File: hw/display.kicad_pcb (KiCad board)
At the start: 2 copper layers, 115.4 x 69.3 mm, 64 parts, among them J1 AMPSEAL_14_POS_776261-1_V, J2 ARM_JTAG_SWD_HEADER_10_PINSMD, J3 HEADER_USART_2_SMD, J4 HEADER_MOLEX_52207-0433, J5 HEADER_MOLEX_54104-4031, U1 MCP2551_SOIC8, U2 ALLIANCE_AS4C4M16SA_TSOP_II, U3 WINDBOND_W25Q32FV_SOIC8_W, U4 LPC1785FBD208_551QFP50, U5 MOSFET-N_2N7002W, U6 MOSFET-N_2N7002W, X1 XTAL_7A-20.000MAAJ-T, X2 XTAL_ABS25-32.768KHZ-T, X3 BUZZER_PKM13EPYH4002-B0

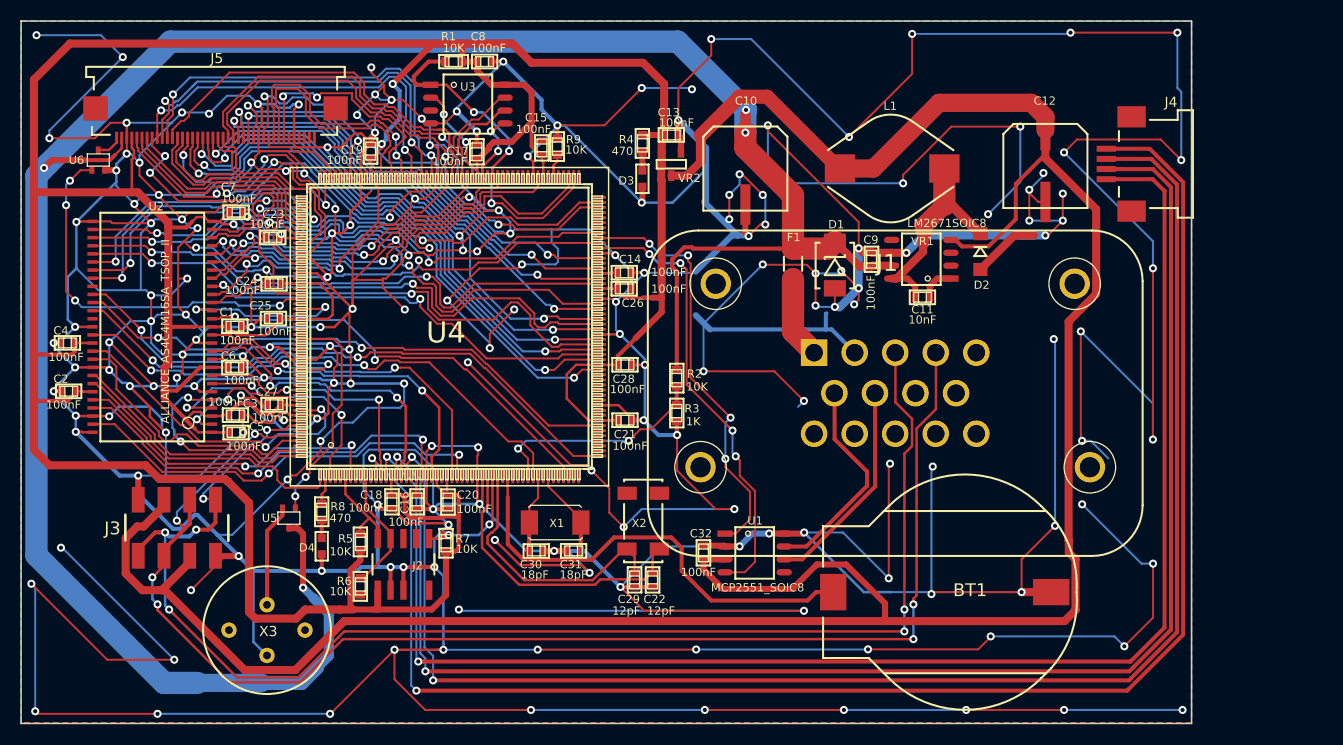
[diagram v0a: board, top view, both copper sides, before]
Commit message: PCB was too big for itead, reduced size and ordered one
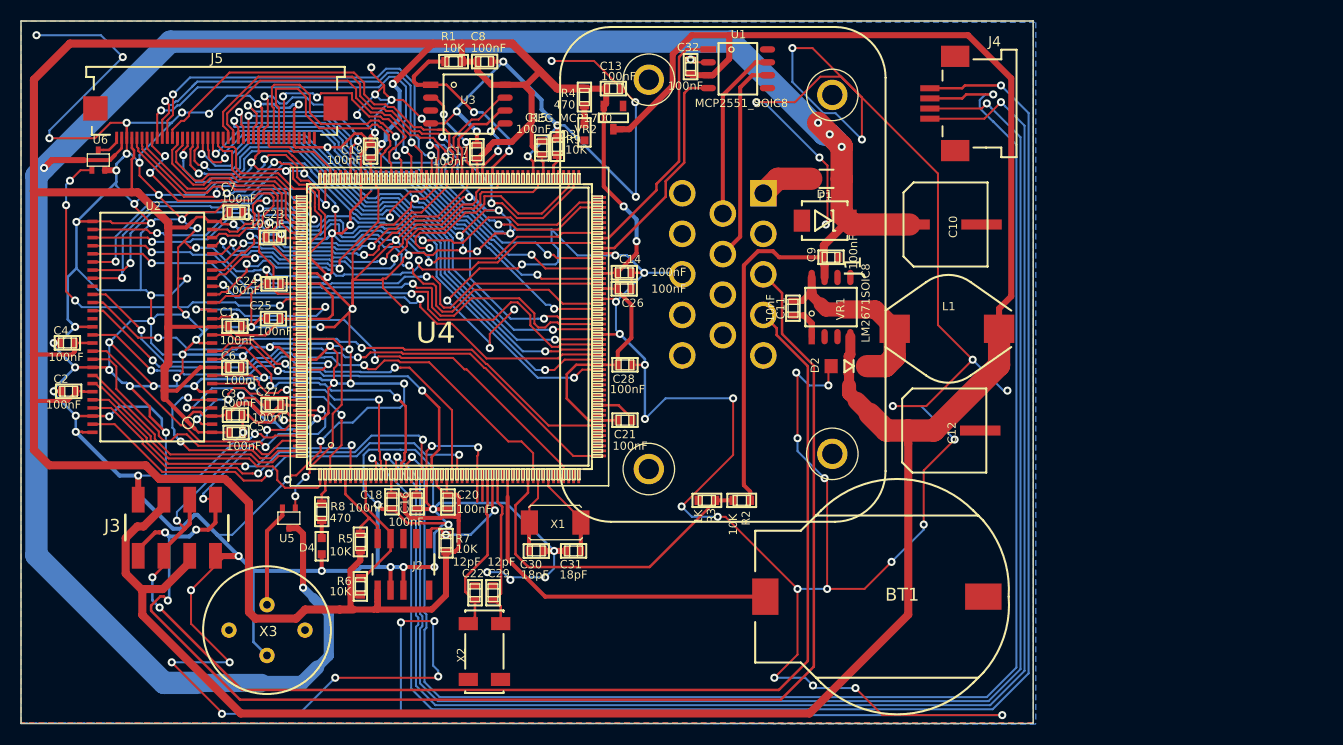
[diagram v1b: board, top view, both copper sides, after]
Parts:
- C10, C12: footprint usevolt:usevolt-CAP_EEE-FK1H470P -> usevolt:CAP_EEE-FK1H470P
- D1: footprint usevolt:usevolt-DO-214AA -> usevolt:DO-214AA
- D2: footprint usevolt:usevolt-DO219AB -> usevolt:DO219AB
- F1: footprint usevolt:usevolt-FUSE_MC36211 -> usevolt:FUSE_MC36211
- J3: footprint usevolt:usevolt-HEADER_4_2_SMD -> usevolt:HEADER_4_2_SMD
- L1: footprint usevolt:usevolt-INDUCTOR_BOURNS_10X13X5MM -> usevolt:INDUCTOR_BOURNS_10X13X5MM
- U1, VR1: footprint usevolt:usevolt-SOIC8 -> usevolt:SOIC8
- U2: footprint usevolt:usevolt-TSOP_II_54_PIN -> usevolt:TSOP_II_54_PIN
- U3: footprint usevolt:usevolt-SOIC8_W -> usevolt:SOIC8_W
- U4: footprint usevolt:usevolt-QFP208 -> usevolt:QFP208
- U5, U6: footprint usevolt:usevolt-SOT323 -> usevolt:SOT323
- VR2: footprint usevolt:usevolt-SOT-23_3-PIN -> usevolt:SOT-23_3-PIN
- X1: footprint usevolt:usevolt-XTAL_7A-20.000MAJ -> usevolt:XTAL_7A-20.000MAJ
- X2: footprint usevolt:usevolt-XTAL_32.768KHZ-T -> usevolt:XTAL_32.768KHZ-T
- moved C32 48.0 mm to (148.6, 60.4)
- moved U1 47.8 mm to (153.2, 60.6)
- moved C12 27.9 mm to (173.6, 96.3), turned to 270 degrees
- moved J1 20.6 mm to (151.8, 80.9), turned to 270 degrees
- moved C10 20.5 mm to (173.7, 75.9), turned to 270 degrees
- moved X2 20.3 mm to (128.2, 118.1), turned to 270 degrees
- moved J4 18.4 mm to (176.5, 64.0)
- moved C22 17.6 mm to (127.3, 112.3), turned to 270 degrees
- moved D2 17.2 mm to (164.2, 89.9), turned to 0 degrees
- moved L1 16.7 mm to (173.9, 86.2), turned to 0 degrees
- moved C29 14.0 mm to (129.1, 112.3), turned to 270 degrees
- moved R2 13.7 mm to (153.6, 103.2), turned to 0 degrees
- moved C11 12.8 mm to (158.7, 84.2), turned to 90 degrees
- moved VR1 10.1 mm to (162.4, 84.1), turned to 90 degrees
- moved R3 9.11 mm to (150.2, 103.2), turned to 0 degrees
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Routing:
- net GND: track 1826.5 -> 1303.4 mm, vias 194 -> 148
- net +5V: track 257.6 -> 230.1 mm
- net /lpc1785_sheet/CAN_RXD: track 44.6 -> 22.3 mm, vias 4 -> 0
- net VDD: track 225.3 -> 243.5 mm, vias 4 -> 5
- net /lpc1785_sheet/CAN_TXD: track 41.6 -> 24.9 mm, vias 4 -> 0
- net +3V3: track 419.3 -> 406.3 mm, vias 4 -> 6
- net /lpc1785_sheet/RTC_X1: track 28.8 -> 16.4 mm
- net /lpc1785_sheet/RTC_X2: track 26.3 -> 15.5 mm
- net /lpc1785_sheet/VDD_SENSE: track 22.3 -> 33.0 mm, vias 2 -> 0
- net /lpc1785_sheet/RTC_BAT: track 44.6 -> 35.2 mm
- net /lpc1785_sheet/TXD: track 139.8 -> 146.5 mm, vias 7 -> 5
- net /lpc1785_sheet/LCD_X_L: track 147.7 -> 152.8 mm
- net /lpc1785_sheet/RXD: track 138.6 -> 134.4 mm, vias 6 -> 4
- net /CANH: track 21.1 -> 17.4 mm
- net /pwr_supply_sheet/VIN: track 8.14 -> 5.32 mm
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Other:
- board size 115.4 x 69.3 mm -> 99.8 x 69.3 mm

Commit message: Changed LCD interface from RGB888 to RGB565
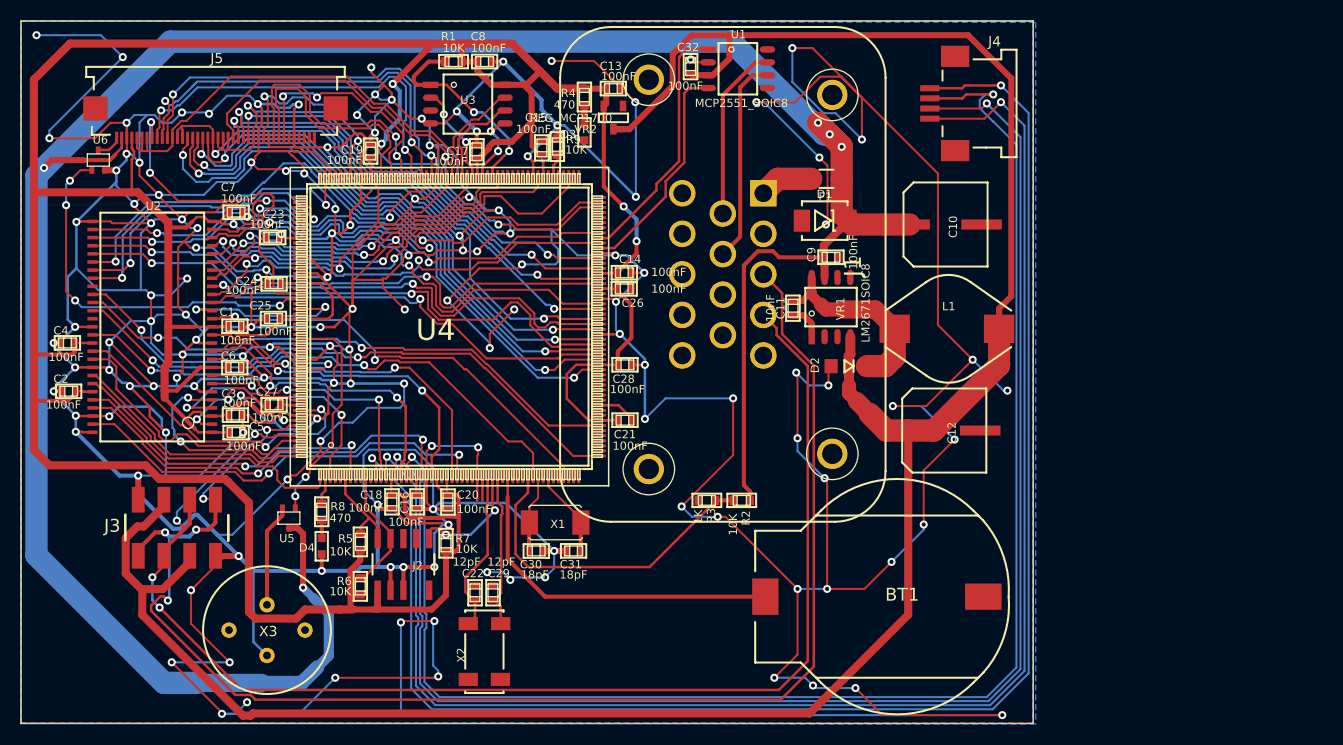
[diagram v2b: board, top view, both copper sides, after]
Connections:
- net /VD10 renamed /G0
- net /VD11 renamed /G1
- net /VD12 renamed /G2
- net /VD13 renamed /G3
- net /VD14 renamed /G4
- net /VD19 renamed /B0
- net /VD20 renamed /B1
- net /VD21 renamed /B2
- net /VD22 renamed /B3
- net /VD3 renamed /R0
- net /VD4 renamed /R1
- net /VD5 renamed /R2
- net /VD6 renamed /R3
- J5 pad 12: /VD7 -> /R4
- J5 pad 13: /VD8 -> /G5
- J5 pad 14: /VD9 -> /G5
- J5 pad 20: /VD15 -> /G5
- J5 pad 21: /VD16 -> /B4
- J5 pad 22: /VD17 -> /B4
- J5 pad 23: /VD18 -> /B4
- J5 pad 28: /VD23 -> /B4
- J5 pad 5: /VD0 -> /R4
- J5 pad 6: /VD1 -> /R4
- J5 pad 7: /VD2 -> /R4
- U4 pad 106: /VD18 -> (no net)
- U4 pad 132: /VD7 -> /R4
- U4 pad 158: /VD17 -> (no net)
- U4 pad 160: /VD16 -> (no net)
- U4 pad 162: /VD9 -> (no net)
- U4 pad 164: /VD8 -> (no net)
- U4 pad 166: /VD1 -> (no net)
- U4 pad 168: /VD0 -> (no net)
- U4 pad 170: /VD2 -> (no net)
- U4 pad 80: /VD15 -> /G5
- U4 pad 92: /VD23 -> /B4
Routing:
- net /G5: track 0.00 -> 57.7 mm, vias 0 -> 2
- net /B4: track 0.00 -> 52.8 mm, vias 0 -> 2
- net /VD15: track 51.1 -> 0.00 mm, vias 2 -> 0
- net /VD18: track 48.5 -> 0.00 mm, vias 2 -> 0
- net /R4: track 0.00 -> 46.3 mm
- net /VD23: track 44.9 -> 0.00 mm, vias 2 -> 0
- net /VD7: track 42.4 -> 0.00 mm
- net /VD0: track 33.5 -> 0.00 mm, vias 2 -> 0
- net /VD1: track 30.3 -> 0.00 mm, vias 2 -> 0
- net /VD2: track 24.8 -> 0.00 mm
- net /VD8: track 20.5 -> 0.00 mm
- net /VD9: track 19.3 -> 0.00 mm
- net /VD17: track 14.2 -> 0.00 mm
- net /VD16: track 13.9 -> 0.00 mm
- net /R0: track 31.6 -> 33.5 mm
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
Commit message: HW revision 3 ordered from itead
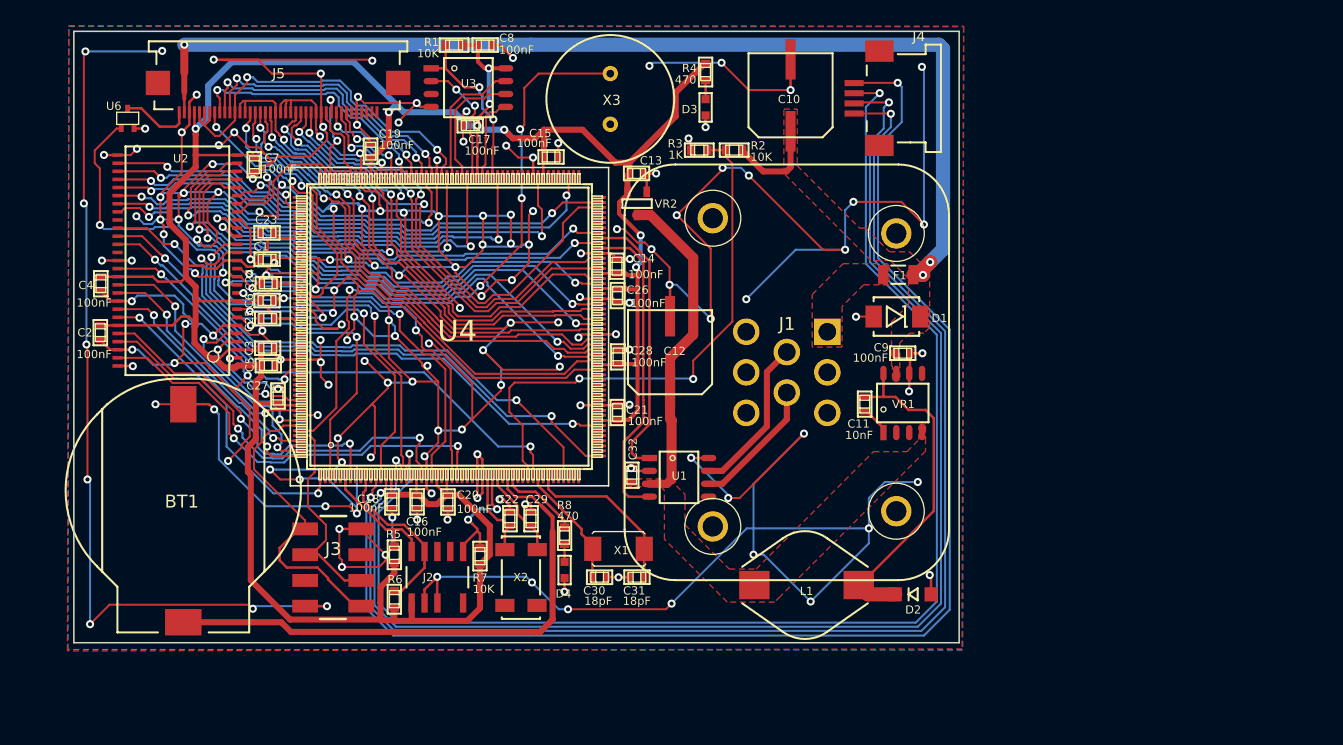
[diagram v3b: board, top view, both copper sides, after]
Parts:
- removed R9: 10K, multicomp:Multicomp-RESC1608X60N
- removed U5: MOSFET-N_2N7002W, usevolt:SOT323
- J1: value AMPSEAL_14_POS_776261-1_V -> AMPSEAL_8_POS_776275-1; footprint usevolt:usevolt-AMPSEAL_14_POS_776261-1 -> usevolt:AMPSEAL_8_POS_776275-1
- moved BT1 81.2 mm to (98.6, 93.7), turned to 270 degrees
- moved X3 62.4 mm to (140.7, 63.6)
- moved C32 40.7 mm to (142.8, 100.7)
- moved U1 40.7 mm to (147.4, 100.9)
- moved R2 34.6 mm to (152.9, 68.6)
- moved R3 34.6 mm to (149.4, 68.6)
- moved L1 28.8 mm to (160.0, 111.5), turned to 180 degrees
- moved C12 28.1 mm to (146.6, 88.5), turned to 0 degrees
- moved D4 24.1 mm to (136.2, 110.0)
- moved R8 24.1 mm to (136.2, 106.6)
- moved D2 23.4 mm to (170.5, 112.4), turned to 180 degrees
- moved C10 19.9 mm to (158.4, 63.2), turned to 0 degrees
- moved J3 15.9 mm to (113.3, 109.8), turned to 0 degrees
- moved D3 12.2 mm to (150.1, 64.4)
- moved R4 12.2 mm to (150.1, 60.9)
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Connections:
- J1 pad P$3: /lpc1785_sheet/TXD -> (no net)
- J1 pad P$4: /lpc1785_sheet/RXD -> /CANH
- J1 pad P$5: (no net) -> /CANL
- J1 pad P$6: /CANH -> (no net)
- J1 pad P$7: /CANL -> (no net)
- J3 pad P$1: /lpc1785_sheet/TXD -> /TXD
- J3 pad P$3: /lpc1785_sheet/RXD -> /RXD
- J3 pad P$4: +5V -> (no net)
- J3 pad P$5: +5V -> (no net)
- J3 pad P$6: /lpc1785_sheet/RXD -> /RXD
- J3 pad P$8: /lpc1785_sheet/TXD -> /TXD
- U2 pad P$20: /A11 -> /BA0
- U2 pad P$21: /A9 -> /BA1
- U2 pad P$22: /A8 -> /A10
- U2 pad P$23: /A7 -> /A0
- U2 pad P$24: /A6 -> /A1
- U2 pad P$25: /A5 -> /A2
- U2 pad P$26: /A4 -> /A3
- U2 pad P$29: /A3 -> /A4
- U2 pad P$30: /A2 -> /A5
- U2 pad P$31: /A1 -> /A6
- U2 pad P$32: /A0 -> /A7
- U2 pad P$33: /A10 -> /A8
- U2 pad P$34: /BA1 -> /A9
- U2 pad P$35: /BA0 -> /A11
- U4 pad 110: /lpc1785_sheet/FORCE_ISP -> (no net)
- U4 pad 185: /lpc1785_sheet/BUZZER -> (no net)
- U4 pad 2: Net-(R8-Pad2) -> (no net)
- U4 pad 202: /lpc1785_sheet/TXD -> /TXD
- U4 pad 203: (no net) -> /lpc1785_sheet/BUZZER
- U4 pad 204: /lpc1785_sheet/RXD -> /RXD
- U4 pad 39: (no net) -> Net-(R8-Pad2)
- X3 pad 1: Net-(U5-PadR) -> /lpc1785_sheet/BUZZER
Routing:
- net GND: track 1302.7 -> 968.6 mm, vias 149 -> 170
- net +5V: track 230.3 -> 32.5 mm
- net /lpc1785_sheet/TXD: track 146.5 -> 0.00 mm, vias 5 -> 0
- net /lpc1785_sheet/RXD: track 134.4 -> 0.00 mm, vias 4 -> 0
- net VDD: track 243.5 -> 115.8 mm, vias 5 -> 3
- net +3V3: track 406.2 -> 320.9 mm, vias 6 -> 8
- net /lpc1785_sheet/BUZZER: track 22.2 -> 61.4 mm, vias 2 -> 4
- net /TXD: track 0.00 -> 30.1 mm
- net /lpc1785_sheet/LCD_X_L: track 152.8 -> 128.1 mm
- net /lpc1785_sheet/LCD_Y_T: track 155.7 -> 133.5 mm
- net /RXD: track 0.00 -> 21.7 mm
- net /lpc1785_sheet/VDD_SENSE: track 33.0 -> 54.2 mm, vias 0 -> 2
- net /BA0: track 32.6 -> 12.5 mm, vias 2 -> 0
- net /BA1: track 30.1 -> 10.4 mm
- net /lpc1785_sheet/LCD_X_R: track 150.6 -> 131.1 mm
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- added copper zone on F.Cu, net +5V
- added copper zone on F.Cu, net /pwr_supply_sheet/VIN
- added copper zone on F.Cu, net VDD
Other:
- board size 99.8 x 69.3 mm -> 87.3 x 60.3 mm
